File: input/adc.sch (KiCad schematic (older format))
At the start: 16 parts, among them U101 LTC2512-24

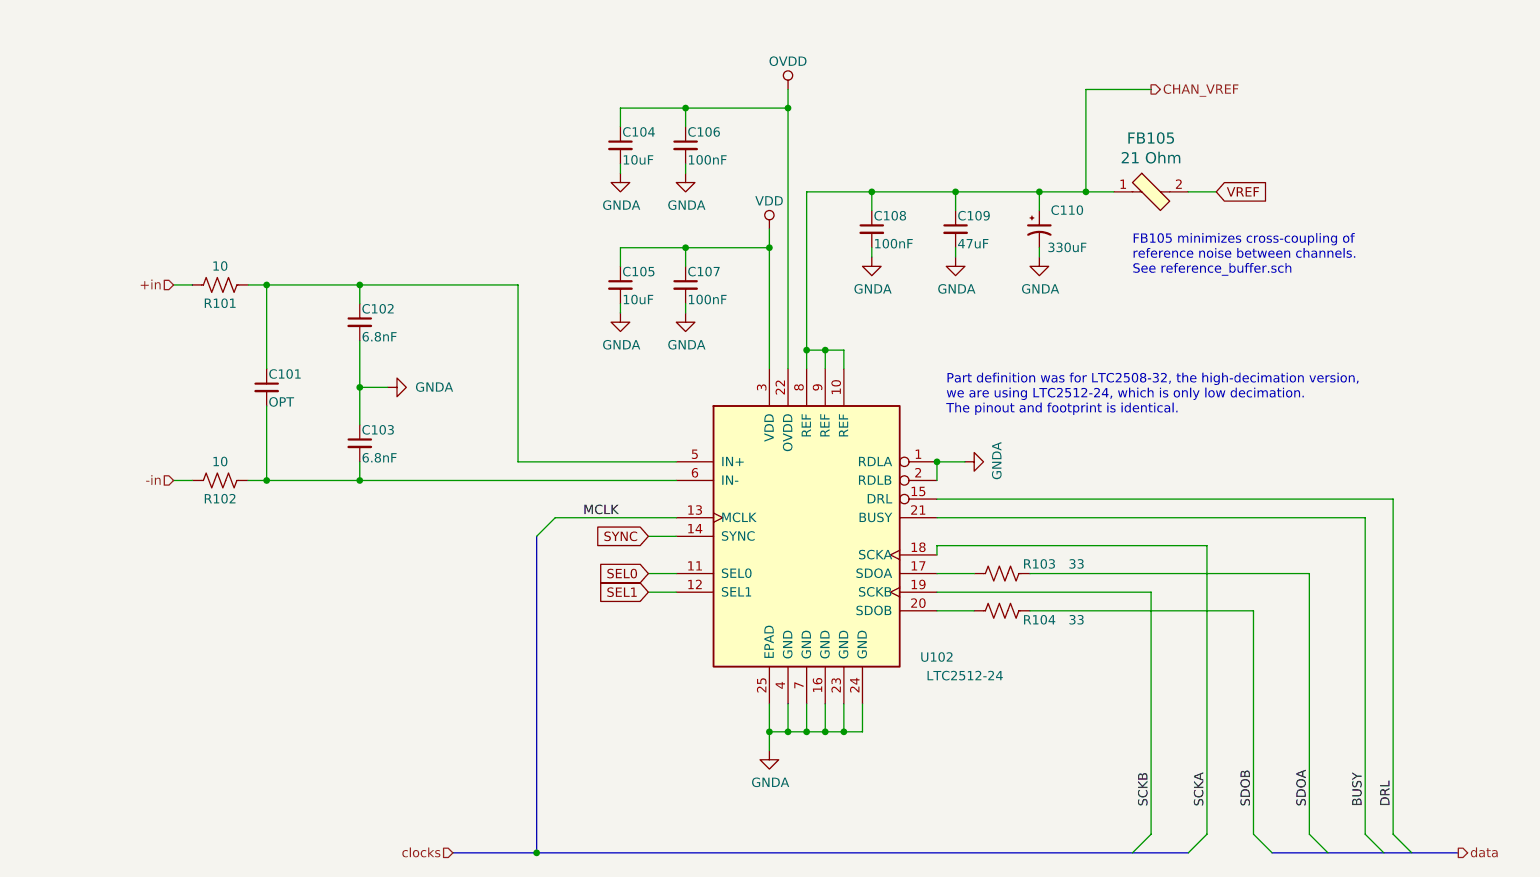
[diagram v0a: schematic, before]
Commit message: Cleanup to get ready to start board layout. I had to get rid off all the bus signals, since in Kicad busses don't work that way.  Added a couple testpoints; many more needed.
Work on component placement in PCB.  I changed DGND to plain GND and "protective earth" to
"earth" (for chassis ground).  Chassis ground is now connected on the board only via a capacitor.
I had to fix the connector footprint to match the pin numbers on the symbol (there was a case
difference).
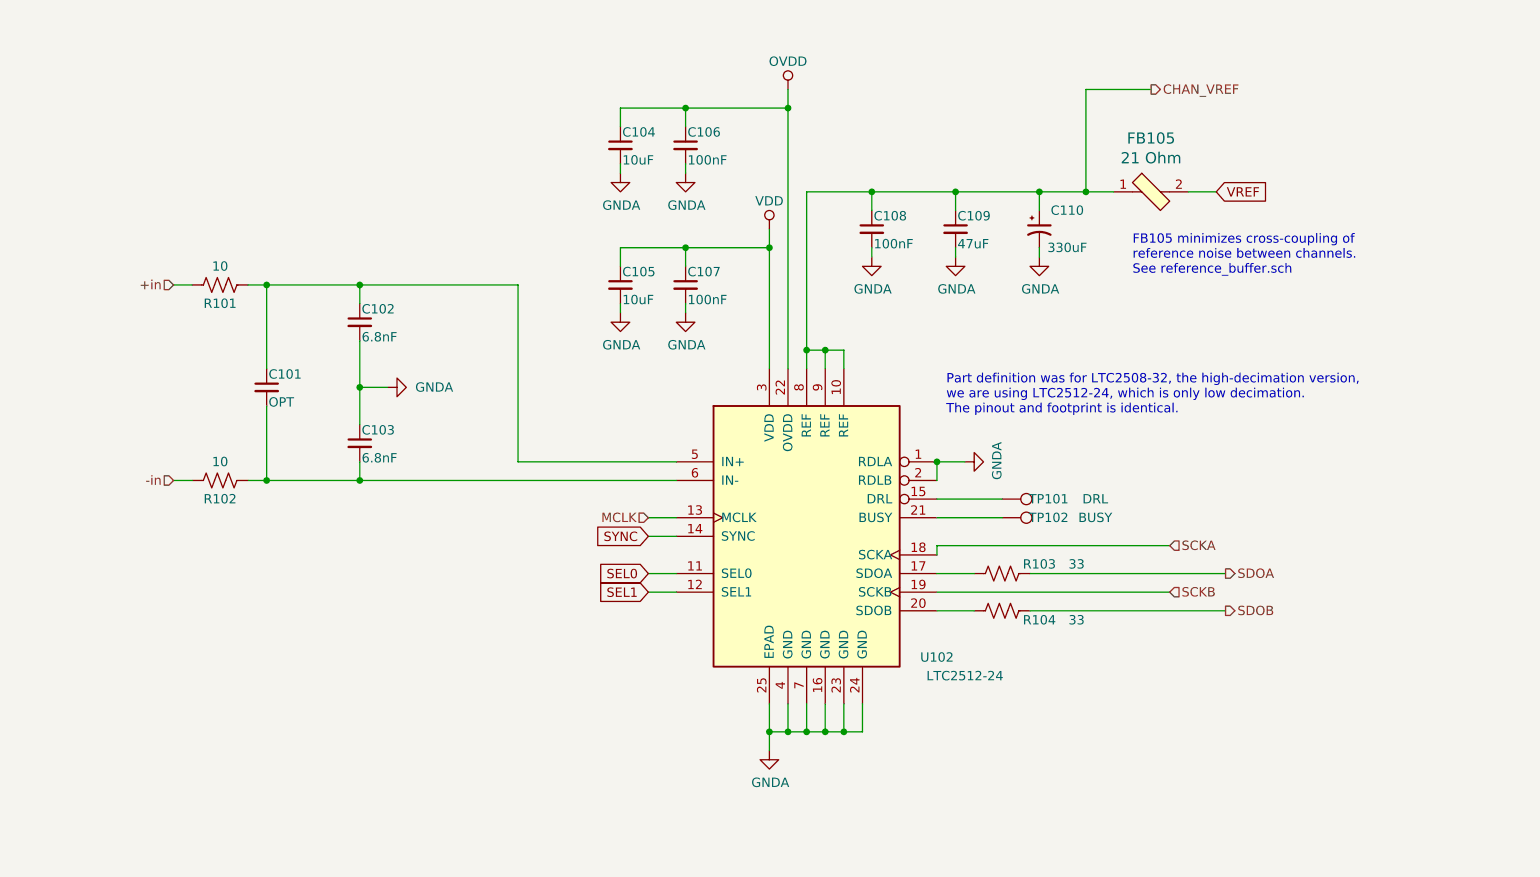
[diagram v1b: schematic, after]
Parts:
- added TP101: DRL, TestPoint:TestPoint_Plated_Hole_D3.0mm, symbol Connector:TestPoint
- added TP102: BUSY, TestPoint:TestPoint_Plated_Hole_D3.0mm, symbol Connector:TestPoint
- FB105: footprint digikey-footprints:0805 -> Inductor_SMD:L_0805_2012Metric
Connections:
- net BUSY: no longer names the net of U101.21 (BUSY)
- net BUSY: now also TP102.1
- net DRL: no longer names the net of U101.15 (DRL)
- net DRL: now also TP101.1

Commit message: Progress on input board layout.  Have adopted 100x280mm eurocard format with connector at the back. Schematic changes are mostly cosmetic.  The working board file is now input/input_board_rear.kicad_pcb
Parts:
- C101, C102, C103: footprint Capacitor_SMD:C_1206_3216Metric -> Capacitor_SMD:C_0805_2012Metric
- TP101, TP102: footprint TestPoint:TestPoint_Plated_Hole_D3.0mm -> TestPoint:TestPoint_THTPad_D1.5mm_Drill0.7mm
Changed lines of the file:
@@
 F 0 "C102" H 4510 2920 50  0000 L CNN
 F 1 "6.8nF" H 4510 2770 50  0000 L CNN
-F 2 "Capacitor_SMD:C_1206_3216Metric" H 4500 2850 50  0001 C CNN
+F 2 "Capacitor_SMD:C_0805_2012Metric" H 4500 2850 50  0001 C CNN
 F 3 "~" H 4500 2850 50  0001 C CNN
 	1    4500 2850
@@
 F 0 "C103" H 4510 3570 50  0000 L CNN
 F 1 "6.8nF" H 4510 3420 50  0000 L CNN
-F 2 "Capacitor_SMD:C_1206_3216Metric" H 4500 3500 50  0001 C CNN
+F 2 "Capacitor_SMD:C_0805_2012Metric" H 4500 3500 50  0001 C CNN
 F 3 "~" H 4500 3500 50  0001 C CNN
 	1    4500 3500
@@
 F 0 "C101" H 4010 3270 50  0000 L CNN
 F 1 "OPT" H 4010 3120 50  0000 L CNN
-F 2 "Capacitor_SMD:C_1206_3216Metric" H 4000 3200 50  0001 C CNN
+F 2 "Capacitor_SMD:C_0805_2012Metric" H 4000 3200 50  0001 C CNN
 F 3 "~" H 4000 3200 50  0001 C CNN
 	1    4000 3200
@@
 F 0 "TP101" V 7950 4050 50  0000 C CNN
 F 1 "DRL" V 7950 4300 50  0000 C CNN
-F 2 "TestPoint:TestPoint_Plated_Hole_D3.0mm" H 8150 3800 50  0001 C CNN
+F 2 "TestPoint:TestPoint_THTPad_D1.5mm_Drill0.7mm" H 8150 3800 50  0001 C CNN
 F 3 "~" H 8150 3800 50  0001 C CNN
 	1    7950 3800
@@
 F 0 "TP102" V 7950 4150 50  0000 C CNN
 F 1 "BUSY" V 7950 4400 50  0000 C CNN
-F 2 "TestPoint:TestPoint_Plated_Hole_D3.0mm" H 8150 3900 50  0001 C CNN
+F 2 "TestPoint:TestPoint_THTPad_D1.5mm_Drill0.7mm" H 8150 3900 50  0001 C CNN
 F 3 "~" H 8150 3900 50  0001 C CNN
 	1    7950 3900

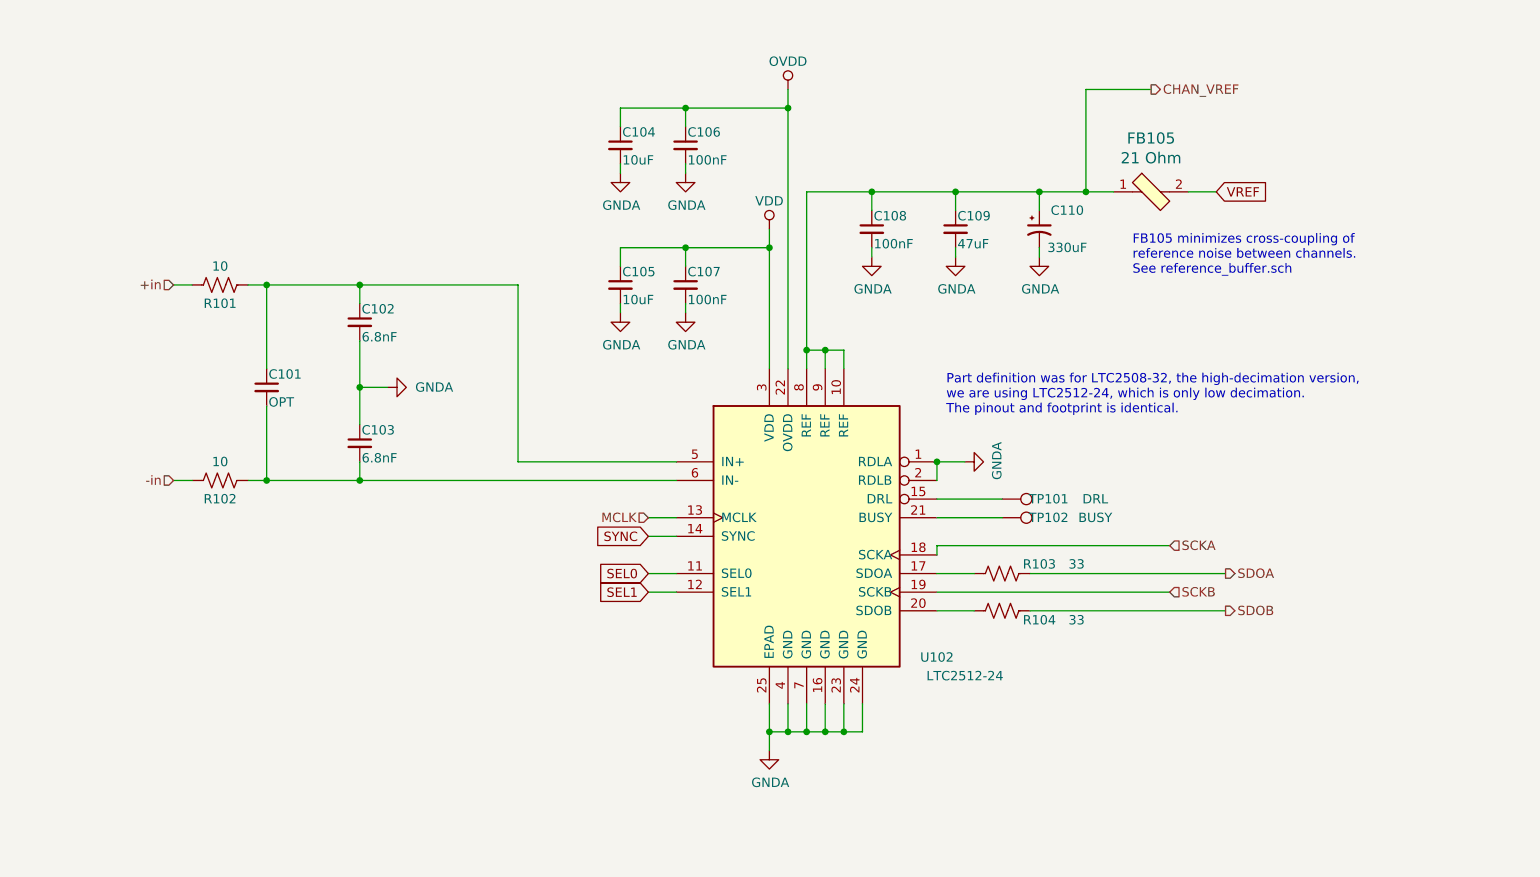
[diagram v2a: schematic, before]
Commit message: Changed board connector to PCIe 8x, added test points, cleanup of component values. Add LVDS Rx termination, bypass caps.
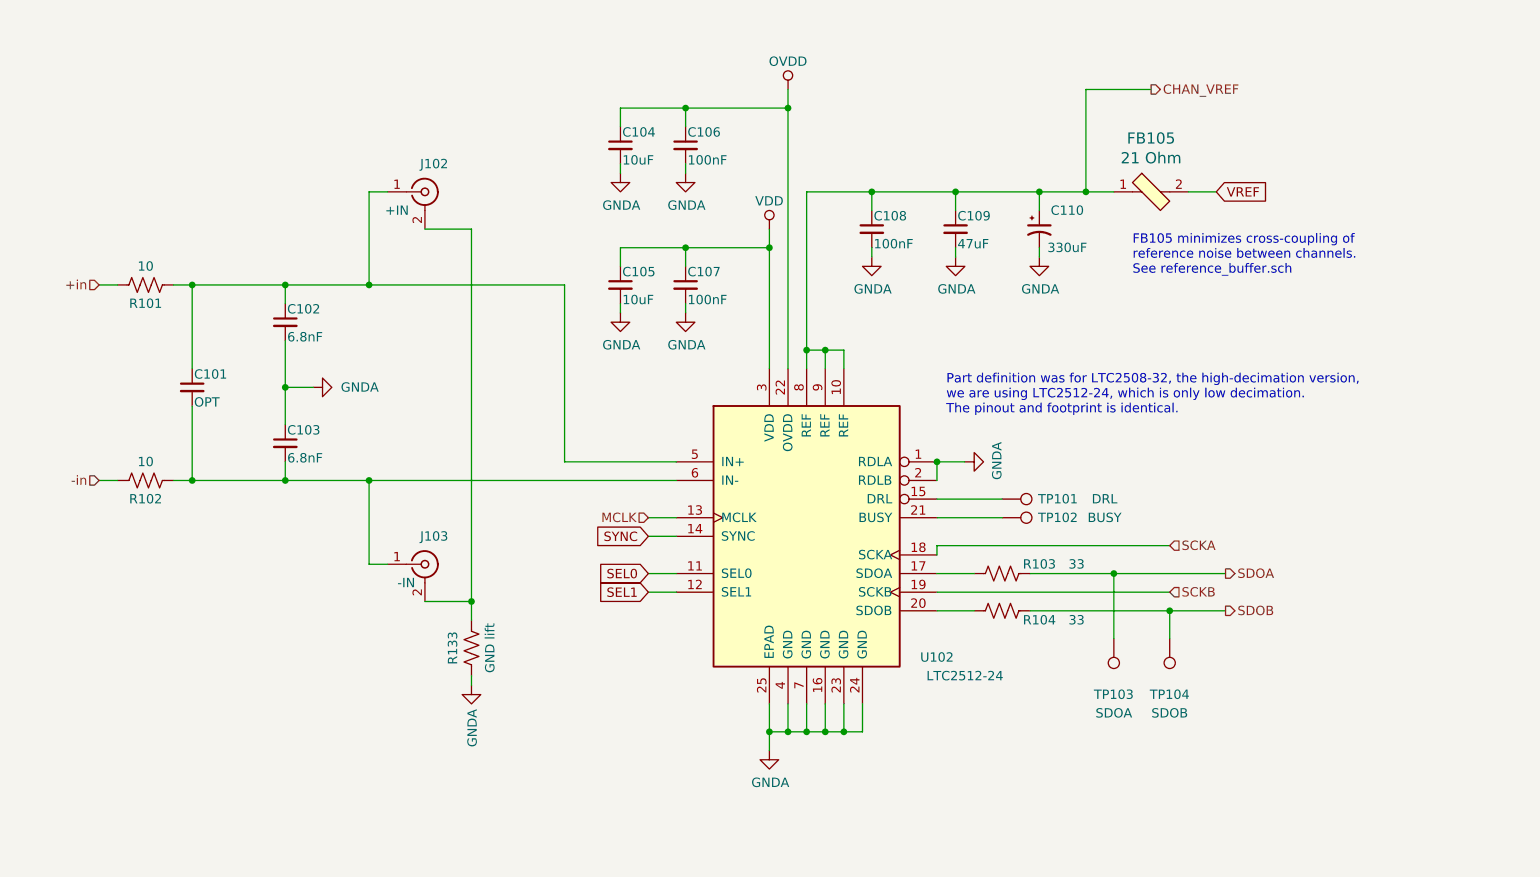
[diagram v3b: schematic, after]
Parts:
- added J102: +IN, Connector_Coaxial:MMCX_Molex_73415-1471_Vertical, symbol Connector:Conn_Coaxial
- added J103: -IN, Connector_Coaxial:MMCX_Molex_73415-1471_Vertical, symbol Connector:Conn_Coaxial
- added R133: GND lift, Resistor_SMD:R_0603_1608Metric, symbol Device:R_US
- added TP103: SDOA, TestPoint:TestPoint_THTPad_D1.5mm_Drill0.7mm, symbol Connector:TestPoint
- added TP104: SDOB, TestPoint:TestPoint_THTPad_D1.5mm_Drill0.7mm, symbol Connector:TestPoint
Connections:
- net GNDA: now also R133.1
- net SDOA: now also TP103.1
- net SDOB: now also TP104.1
- net at C101.2, C103.2, R102.1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: now also J103.1 (In)
- net at C101.1, C102.1, R101.1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: now also J102.1 (In)
- new net: J102.2 (Ext), J103.2 (Ext), R133.2
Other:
- moved on the sheet: C101, C102, C103, R101, R102
